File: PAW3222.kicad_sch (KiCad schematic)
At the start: 7 parts, among them J1 Conn_01x06_Socket, U1 PAW3220LU

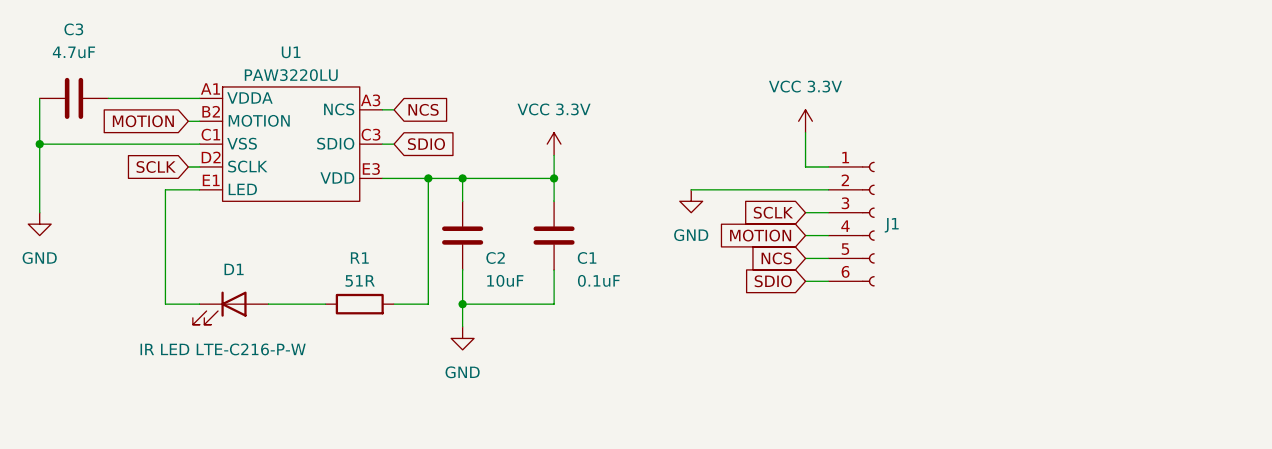
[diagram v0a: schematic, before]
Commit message: update pcb to ffc cable connector
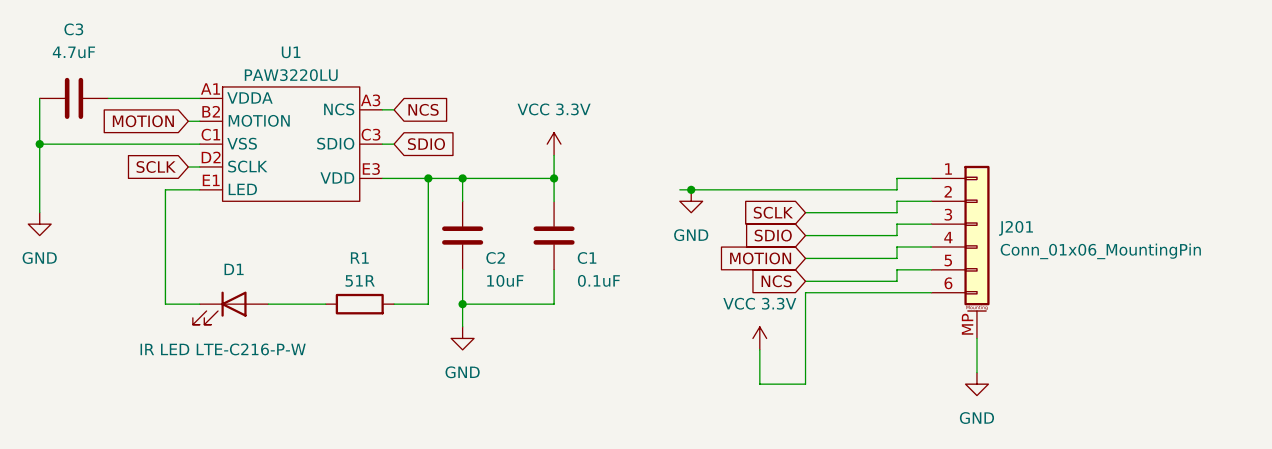
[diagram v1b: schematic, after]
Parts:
- removed J1: Conn_01x06_Socket, Connector_PinHeader_1.27mm:PinHeader_1x06_P1.27mm_Vertical, symbol Connector:Conn_01x06_Socket
- added J201: Conn_01x06_MountingPin, paw3222:GT-F0501SR10-06S1101, symbol Connector_Generic_MountingPin:Conn_01x06_MountingPin
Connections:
- net GND: now also J201.1 (Pin_1), J201.MP (MountPin)
- net MOTION: now also J201.4 (Pin_4)
- net NCS: now also J201.5 (Pin_5)
- net SCLK: now also J201.2 (Pin_2)
- net SDIO: now also J201.3 (Pin_3)
- net VCC 3.3V: now also J201.6 (Pin_6)

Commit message: flip pin out
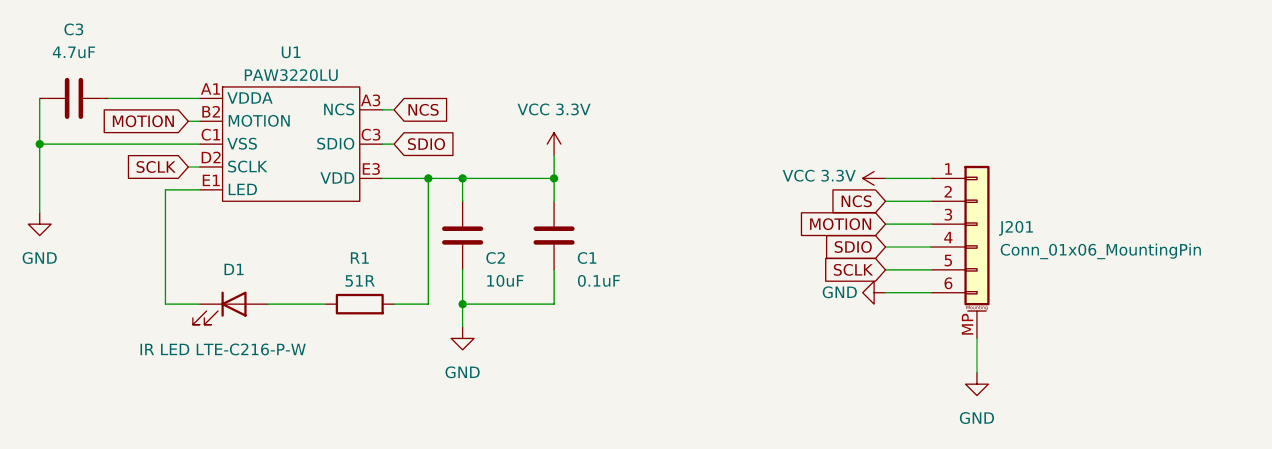
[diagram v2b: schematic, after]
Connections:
- net GND: now also J201.6 (Pin_6); no longer J201.1 (Pin_1)
- net MOTION: now also J201.3 (Pin_3); no longer J201.4 (Pin_4)
- net NCS: now also J201.2 (Pin_2); no longer J201.5 (Pin_5)
- net SCLK: now also J201.5 (Pin_5); no longer J201.2 (Pin_2)
- net SDIO: now also J201.4 (Pin_4); no longer J201.3 (Pin_3)
- net VCC 3.3V: now also J201.1 (Pin_1); no longer J201.6 (Pin_6)
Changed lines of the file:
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@@
-	)
-	(junction
-		(at 168.91 90.17)
-		(diameter 0)
-		(color 0 0 0 0)
 	)
 	(junction
@@
 	(wire
 		(pts
-			(xy 191.77 95.25) (xy 191.77 93.98)
-		)
-		(stroke
-			(width 0)
-			(type default)
-		)
-	)
-	(wire
-		(pts
 			(xy 110.49 90.17) (xy 114.3 90.17)
 		)
@@
 	(wire
 		(pts
-			(xy 191.77 99.06) (xy 195.58 99.06)
+			(xy 190.5 99.06) (xy 195.58 99.06)
 		)
 		(stroke
@@
 	(wire
 		(pts
-			(xy 191.77 97.79) (xy 191.77 96.52)
-		)
-		(stroke
-			(width 0)
-			(type default)
-		)
-	)
-	(wire
-		(pts
 			(xy 96.52 85.09) (xy 96.52 92.71)
 		)
@@
 	(wire
 		(pts
-			(xy 181.61 95.25) (xy 191.77 95.25)
-		)
-		(stroke
-			(width 0)
-			(type default)
-		)
-	)
-	(wire
-		(pts
-			(xy 191.77 100.33) (xy 191.77 99.06)
-		)
-		(stroke
-			(width 0)
-			(type default)
-		)
-	)
-	(wire
-		(pts
 			(xy 143.51 88.9) (xy 143.51 91.44)
 		)
@@
 	(wire
 		(pts
-			(xy 181.61 111.76) (xy 181.61 101.6)
-		)
-		(stroke
-			(width 0)
-			(type default)
-		)
-	)
-	(wire
-		(pts
 			(xy 96.52 85.09) (xy 114.3 85.09)
 		)
@@
 	(wire
 		(pts
-			(xy 191.77 88.9) (xy 195.58 88.9)
-		)
-		(stroke
-			(width 0)
-			(type default)
-		)
-	)
-	(wire
-		(pts
-			(xy 181.61 100.33) (xy 191.77 100.33)
+			(xy 190.5 88.9) (xy 195.58 88.9)
 		)
 		(stroke
@@
 	(wire
 		(pts
-			(xy 191.77 93.98) (xy 195.58 93.98)
-		)
-		(stroke
-			(width 0)
-			(type default)
-		)
-	)
-	(wire
-		(pts
-			(xy 181.61 101.6) (xy 195.58 101.6)
-		)
-		(stroke
-			(width 0)
-			(type default)
-		)
-	)
-	(wire
-		(pts
-			(xy 176.53 111.76) (xy 176.53 107.95)
-		)
-		(stroke
-			(width 0)
-			(type default)
-		)
-	)
-	(wire
-		(pts
-			(xy 191.77 96.52) (xy 195.58 96.52)
+			(xy 190.5 93.98) (xy 195.58 93.98)
+		)
+		(stroke
+			(width 0)
+			(type default)
+		)
+	)
+	(wire
+		(pts
+			(xy 190.5 101.6) (xy 195.58 101.6)
+		)
+		(stroke
+			(width 0)
+			(type default)
+		)
+	)
+	(wire
+		(pts
+			(xy 190.5 96.52) (xy 195.58 96.52)
 		)
 		(stroke
@@
 	(wire
 		(pts
-			(xy 168.91 90.17) (xy 191.77 90.17)
-		)
-		(stroke
-			(width 0)
-			(type default)
-		)
-	)
-	(wire
-		(pts
-			(xy 191.77 92.71) (xy 191.77 91.44)
-		)
-		(stroke
-			(width 0)
-			(type default)
-		)
-	)
-	(wire
-		(pts
-			(xy 191.77 90.17) (xy 191.77 88.9)
-		)
-		(stroke
-			(width 0)
-			(type default)
-		)
-	)
-	(wire
-		(pts
 			(xy 110.49 102.87) (xy 110.49 90.17)
 		)
@@
 	(wire
 		(pts
+			(xy 190.5 91.44) (xy 195.58 91.44)
+		)
+		(stroke
+			(width 0)
+			(type default)
+		)
+	)
+	(wire
+		(pts
 			(xy 135.89 85.09) (xy 134.62 85.09)
 		)
@@
 	(wire
 		(pts
-			(xy 167.64 90.17) (xy 168.91 90.17)
-		)
-		(stroke
-			(width 0)
-			(type default)
-		)
-	)
-	(wire
-		(pts
-			(xy 181.61 92.71) (xy 191.77 92.71)
-		)
-		(stroke
-			(width 0)
-			(type default)
-		)
-	)
-	(wire
-		(pts
 			(xy 114.3 82.55) (xy 113.03 82.55)
 		)
@@
 	(wire
 		(pts
-			(xy 181.61 111.76) (xy 176.53 111.76)
-		)
-		(stroke
-			(width 0)
-			(type default)
-		)
-	)
-	(wire
-		(pts
 			(xy 104.14 80.01) (xy 114.3 80.01)
 		)
@@
 	(wire
 		(pts
-			(xy 181.61 97.79) (xy 191.77 97.79)
-		)
-		(stroke
-			(width 0)
-			(type default)
-		)
-	)
-	(wire
-		(pts
 			(xy 153.67 102.87) (xy 143.51 102.87)
 		)
@@
 		(pts
 			(xy 121.92 102.87) (xy 128.27 102.87)
-		)
-		(stroke
-			(width 0)
-			(type default)
-		)
-	)
-	(wire
-		(pts
-			(xy 191.77 91.44) (xy 195.58 91.44)
 		)
 		(stroke
@@
 	(global_label "SCLK"
 		(shape input)
-		(at 181.61 92.71 180)
+		(at 190.5 99.06 180)
 		(fields_autoplaced yes)
 		(effects
@@
 		)
 		(property "Intersheetrefs" "${INTERSHEET_REFS}"
-			(at 173.8472 92.71 0)
+			(at 182.7372 99.06 0)
 			(effects
 				(font
@@
 	(global_label "NCS"
 		(shape input)
-		(at 181.61 100.33 180)
+		(at 190.5 91.44 180)
 		(fields_autoplaced yes)
 		(effects
@@
 		)
 		(property "Intersheetrefs" "${INTERSHEET_REFS}"
-			(at 174.8148 100.33 0)
+			(at 183.7048 91.44 0)
 			(effects
 				(font
@@
 	(global_label "SDIO"
 		(shape input)
-		(at 181.61 95.25 180)
+		(at 190.5 96.52 180)
 		(fields_autoplaced yes)
 		(effects
@@
 		)
 		(property "Intersheetrefs" "${INTERSHEET_REFS}"
-			(at 174.21 95.25 0)
+			(at 183.1 96.52 0)
 			(effects
 				(font
@@
 	(global_label "MOTION"
 		(shape input)
-		(at 181.61 97.79 180)
+		(at 190.5 93.98 180)
 		(fields_autoplaced yes)
 		(effects
@@
 		)
 		(property "Intersheetrefs" "${INTERSHEET_REFS}"
-			(at 171.6095 97.79 0)
+			(at 180.4995 93.98 0)
 			(effects
 				(font
@@
 	(symbol
 		(lib_id "power:VCC")
-		(at 176.53 107.95 0)
+		(at 190.5 88.9 90)
 		(unit 1)
 		(exclude_from_sim no)
@@
 		(on_board yes)
 		(dnp no)
-		(fields_autoplaced yes)
 		(property "Reference" "#PWR07"
-			(at 176.53 111.76 0)
+			(at 194.31 88.9 0)
 			(effects
 				(font
@@
 		)
 		(property "Value" "VCC 3.3V"
-			(at 176.53 102.87 0)
+			(at 183.134 88.646 90)
 			(effects
 				(font
@@
 		)
 		(property "Footprint" ""
-			(at 176.53 107.95 0)
+			(at 190.5 88.9 0)
 			(effects
 				(font
@@
 		)
 		(property "Datasheet" ""
-			(at 176.53 107.95 0)
+			(at 190.5 88.9 0)
 			(effects
 				(font
@@
 		)
 		(property "Description" "Power symbol creates a global label with name \"VCC\""
-			(at 176.53 107.95 0)
+			(at 190.5 88.9 0)
 			(effects
 				(font
@@
 	(symbol
 		(lib_id "power:GND")
-		(at 168.91 90.17 0)
+		(at 190.5 101.6 270)
 		(unit 1)
 		(exclude_from_sim no)
@@
 		(on_board yes)
 		(dnp no)
-		(fields_autoplaced yes)
 		(property "Reference" "#PWR06"
-			(at 168.91 96.52 0)
+			(at 184.15 101.6 0)
 			(effects
 				(font
@@
 		)
 		(property "Value" "GND"
-			(at 168.91 95.25 0)
+			(at 185.42 101.6 90)
 			(effects
 				(font
@@
 		)
 		(property "Footprint" ""
-			(at 168.91 90.17 0)
+			(at 190.5 101.6 0)
 			(effects
 				(font
@@
 		)
 		(property "Datasheet" ""
-			(at 168.91 90.17 0)
+			(at 190.5 101.6 0)
 			(effects
 				(font
@@
 		)
 		(property "Description" "Power symbol creates a global label with name \"GND\" , ground"
-			(at 168.91 90.17 0)
-			(effects
-				(font
+			(at 190.5 101.6 0)
+			(effects
+				(font
